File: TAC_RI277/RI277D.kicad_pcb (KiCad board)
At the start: 2 copper layers, 62 x 37 mm, 9 parts, among them J1 Ribbon Cable, J2 Tape Return

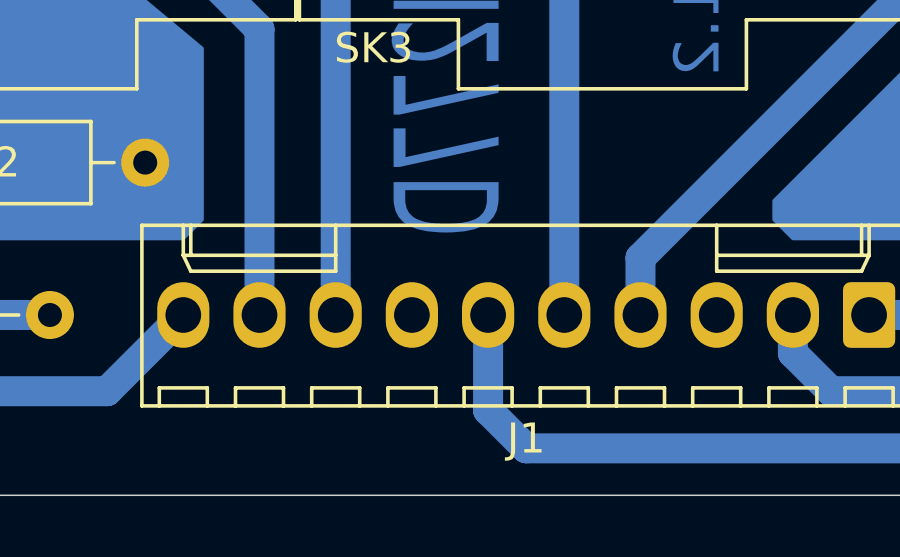
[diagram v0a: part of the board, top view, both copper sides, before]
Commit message: included RI277 to diagram, fixed missing bridge pin 6-7 on RI277D
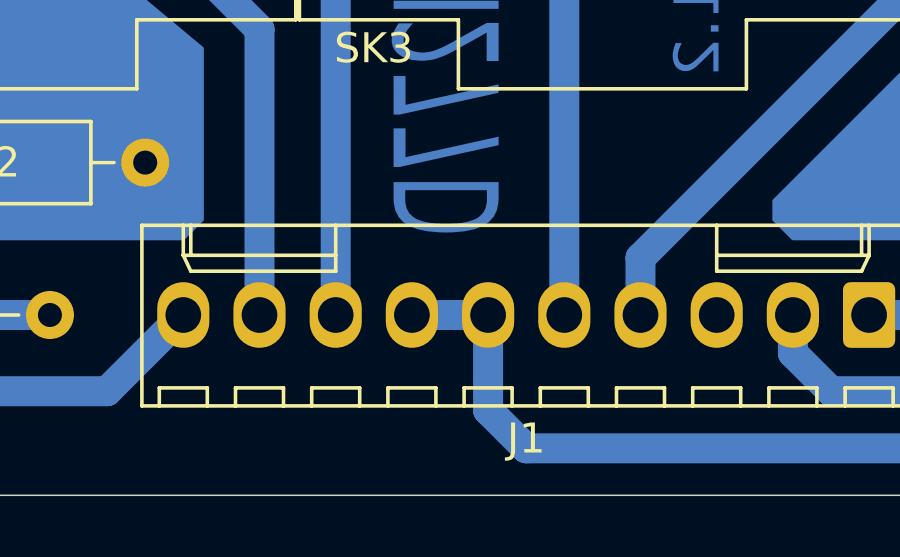
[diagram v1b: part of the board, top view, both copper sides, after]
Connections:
- J1 pad 7: Net-(J1-Pad7) -> Net-(J1-Pad6)
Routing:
- net Net-(J1-Pad6): track 57.3 -> 59.8 mm
